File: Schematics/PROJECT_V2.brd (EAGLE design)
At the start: 251.5 x 194.3 mm, 47 parts

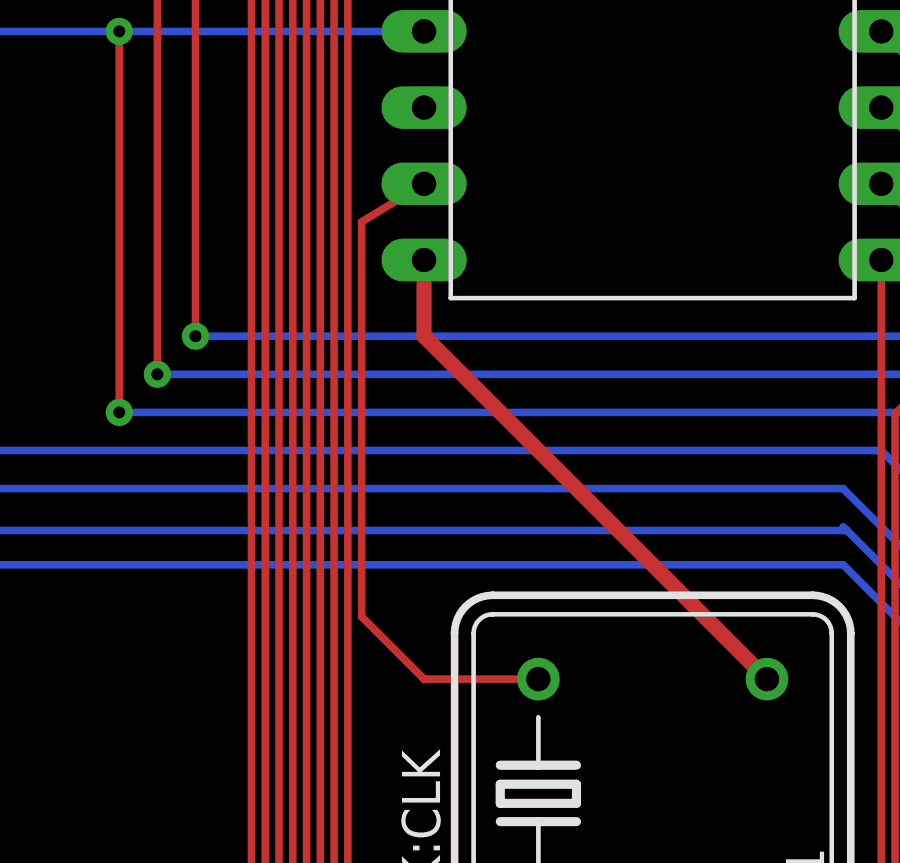
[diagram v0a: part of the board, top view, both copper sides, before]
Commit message: Added git ignore, cleaned up some files, commited project paper (ECEN 4330 Final Paper.pdf), added adjuted bom
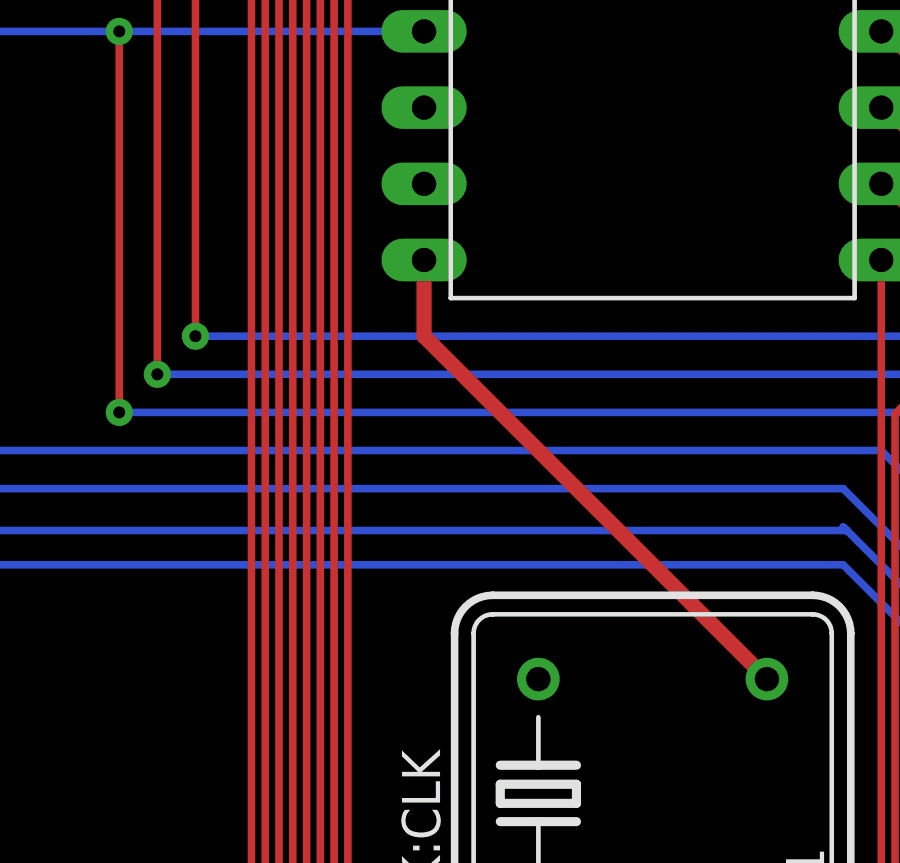
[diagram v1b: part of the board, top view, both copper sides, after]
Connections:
- net CLKSIG renamed N$1
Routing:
- net N$1: track 22.3 -> 0.00 mm
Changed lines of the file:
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@@
 <wire x1="138.43" y1="30.48" x2="127" y2="41.91" width="0.508" layer="1"/>
 <wire x1="127" y1="41.91" x2="127" y2="44.45" width="0.508" layer="1"/>
+<wire x1="90.424" y1="165.862" x2="86.741" y2="160.274" width="0" layer="19" extent="1-1"/>
+<wire x1="61.214" y1="174.752" x2="86.741" y2="160.274" width="0" layer="19" extent="1-1"/>
+<wire x1="38.735" y1="167.386" x2="61.214" y2="174.752" width="0" layer="19" extent="1-1"/>
+<wire x1="11.684" y1="178.842" x2="38.735" y2="167.386" width="0" layer="19" extent="1-1"/>
+<wire x1="8.684" y1="183.642" x2="11.684" y2="178.842" width="0" layer="19" extent="1-1"/>
+<wire x1="71.882" y1="121.92" x2="86.741" y2="160.274" width="0" layer="19" extent="1-1"/>
+<wire x1="86.741" y1="83.058" x2="71.882" y2="121.92" width="0" layer="19" extent="1-1"/>
+<wire x1="71.882" y1="44.45" x2="86.741" y2="83.058" width="0" layer="19" extent="1-1"/>
+<wire x1="54.61" y1="25.4" x2="64.643" y2="31.75" width="0" layer="19" extent="1-1"/>
+<wire x1="62.23" y1="6.35" x2="49.53" y2="20.32" width="0" layer="19" extent="1-1"/>
+<wire x1="30.734" y1="6.858" x2="49.53" y2="20.32" width="0" layer="19" extent="1-1"/>
+<wire x1="23.114" y1="6.858" x2="30.734" y2="6.858" width="0" layer="19" extent="1-1"/>
+<wire x1="18.034" y1="21.971" x2="23.114" y2="6.858" width="0" layer="19" extent="1-1"/>
+<wire x1="14.224" y1="28.448" x2="18.034" y2="21.971" width="0" layer="19" extent="1-1"/>
+<wire x1="25.527" y1="36.322" x2="14.224" y2="28.448" width="0" layer="19" extent="1-1"/>
+<wire x1="114.3" y1="128.143" x2="86.741" y2="160.274" width="0" layer="19" extent="1-1"/>
+<wire x1="119.38" y1="125.73" x2="114.3" y2="128.143" width="0" layer="19" extent="1-1"/>
+<wire x1="142.24" y1="125.73" x2="119.38" y2="125.73" width="0" layer="19" extent="1-1"/>
+<wire x1="145.161" y1="96.774" x2="142.24" y2="125.73" width="0" layer="19" extent="1-1"/>
+<wire x1="165.1" y1="95.25" x2="145.161" y2="96.774" width="0" layer="19" extent="1-1"/>
+<wire x1="167.513" y1="100.33" x2="165.1" y2="95.25" width="0" layer="19" extent="1-1"/>
+<wire x1="165.1" y1="72.39" x2="165.1" y2="95.25" width="0" layer="19" extent="1-1"/>
+<wire x1="142.24" y1="69.85" x2="165.1" y2="69.85" width="0" layer="19" extent="1-1"/>
+<wire x1="189.23" y1="110.617" x2="167.513" y2="100.33" width="0" layer="19" extent="1-1"/>
+<wire x1="194.31" y1="108.204" x2="189.23" y2="110.617" width="0" layer="19" extent="1-1"/>
+<wire x1="217.17" y1="108.204" x2="194.31" y2="108.204" width="0" layer="19" extent="1-1"/>
+<wire x1="229.87" y1="115.4938" x2="217.17" y2="108.204" width="0" layer="19" extent="1-1"/>
+<wire x1="127" y1="44.45" x2="142.24" y2="69.85" width="0" layer="19" extent="1-1"/>
+<wire x1="165.1" y1="34.29" x2="138.43" y2="30.48" width="0" layer="19" extent="1-1"/>
+<wire x1="38.481" y1="90.424" x2="71.882" y2="121.92" width="0" layer="19" extent="1-1"/>
+<wire x1="23.13" y1="121.682" x2="38.481" y2="90.424" width="0" layer="19" extent="1-1"/>
+<wire x1="144.907" y1="187.96" x2="90.424" y2="165.862" width="0" layer="19" extent="1-1"/>
+<wire x1="157.48" y1="186.69" x2="144.907" y2="187.96" width="0" layer="19" extent="1-1"/>
 </signal>
 <signal name="VCC">
@@
 <wire x1="23.700625" y1="188.33128125" x2="31.62928125" y2="188.33128125" width="0.508" layer="1"/>
 </signal>
-<signal name="CLKSIG">
+<signal name="N$1">
+<contactref element="MC:UC" pad="19"/>
 <contactref element="CLK:CLK" pad="5"/>
-<contactref element="MC:UC" pad="19"/>
-<wire x1="130.81" y1="30.48" x2="127" y2="30.48" width="0.254" layer="1"/>
-<wire x1="124.919" y1="32.561" x2="124.919" y2="45.72" width="0.254" layer="1"/>
-<wire x1="127" y1="30.48" x2="124.919" y2="32.561" width="0.254" layer="1"/>
-<wire x1="124.919" y1="45.72" x2="127" y2="46.99" width="0.254" layer="1"/>
+<wire x1="130.81" y1="30.48" x2="127" y2="46.99" width="0" layer="19" extent="1-1"/>
 </signal>
 </signals>
